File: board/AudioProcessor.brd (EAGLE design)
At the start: 49.5 x 45.7 mm, 50 parts, among them IC1 LP2951, IC2 ATTINY24/44/84-SSU, IC3 TDA7439DS, IC4 LP2951, J1 PINHD-1X3-JST-PH, J2 PINHD-1X3-JST-PH, J3 PINHD-1X3-JST-PH, J4 PINHD-1X3-JST-PH, J5 PINHD-1X6-JST-PH, J6 PINHD-1X3-JST-PH

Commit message: Removed unnecessary output biasing
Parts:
- removed C4, C8: 0.47uF, SaintGimp:CAPACITOR-5MM
- removed R6, R7, R8, R9: 10K, SaintGimp:RESISTOR-0805
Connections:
- removed net L-OUT-BIASED: C8.2, J5.2, R7.2, R9.1
- removed net R-OUT-BIASED: C4.2, J5.5, R6.2, R8.1
- net +3V3: no longer R8.2, R9.2
- net GND: no longer R6.1, R7.1
- net L-OUT: now also J5.2; no longer C8.1
- net R-OUT: now also J5.5; no longer C4.1
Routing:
- net +3V3: track 126.0 -> 100.0 mm
- net L-OUT-BIASED: track 13.2 -> 0.00 mm
- net R-OUT-BIASED: track 13.2 -> 0.00 mm
- net GND: track 44.7 -> 36.3 mm
- net L-OUT: track 20.6 -> 16.8 mm
- net R-OUT: track 14.9 -> 13.8 mm
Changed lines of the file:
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@@
 <attribute name="NAME" x="32.258" y="19.304" size="0.8128" layer="25" rot="R270"/>
-</element>
-<element name="C8" library="SaintGimp" package="CAPACITOR-5MM" value="0.47uF" x="11.43" y="15.24" smashed="yes" rot="R180">
-<attribute name="NAME" x="10.668" y="12.954" size="0.8128" layer="25"/>
-</element>
-<element name="C4" library="SaintGimp" package="CAPACITOR-5MM" value="0.47uF" x="11.43" y="25.4" smashed="yes" rot="R180">
-<attribute name="NAME" x="10.668" y="26.924" size="0.8128" layer="25"/>
 </element>
 <element name="C6" library="SaintGimp" package="CAPACITOR-1206" value="10uF" x="34.925" y="29.21" smashed="yes">
@@
 <attribute name="NAME" x="31.9405" y="7.747" size="0.8128" layer="25" rot="R270"/>
 </element>
-<element name="R6" library="SaintGimp" package="RESISTOR-0805" value="10K" x="8.89" y="21.59" smashed="yes">
-<attribute name="NAME" x="8.128" y="22.6695" size="0.8128" layer="25"/>
-</element>
 <element name="R3" library="SaintGimp" package="RESISTOR-0805" value="10K" x="35.56" y="33.02" smashed="yes" rot="R180">
 <attribute name="NAME" x="35.56" y="33.9725" size="0.8128" layer="25" rot="R180" align="top-center"/>
@@
 <element name="R11" library="SaintGimp" package="RESISTOR-0805" value="100K" x="40.64" y="19.05" smashed="yes" rot="R180">
 <attribute name="NAME" x="41.656" y="17.9705" size="0.8128" layer="25" rot="R180"/>
-</element>
-<element name="R9" library="SaintGimp" package="RESISTOR-0805" value="10K" x="13.97" y="19.05" smashed="yes">
-<attribute name="NAME" x="13.208" y="17.0815" size="0.8128" layer="25"/>
-</element>
-<element name="R7" library="SaintGimp" package="RESISTOR-0805" value="10K" x="8.89" y="19.05" smashed="yes">
-<attribute name="NAME" x="8.128" y="17.0815" size="0.8128" layer="25"/>
-</element>
-<element name="R8" library="SaintGimp" package="RESISTOR-0805" value="10K" x="13.97" y="21.59" smashed="yes">
-<attribute name="NAME" x="13.208" y="22.6695" size="0.8128" layer="25"/>
 </element>
 <element name="J6" library="SaintGimp" package="JST-B3B-PH" value="PINHD-1X3-JST-PH" x="45.72" y="24.765" smashed="yes" rot="R90">
@@
 <contactref element="R13" pad="1"/>
 <contactref element="C10" pad="2"/>
-<contactref element="R7" pad="1"/>
-<contactref element="R6" pad="1"/>
 <contactref element="C5" pad="2"/>
 <contactref element="J5" pad="4"/>
@@
 </polygon>
 <via x="35.052" y="1.27" extent="1-16" drill="0.5"/>
-<wire x1="7.89" y1="19.05" x2="7.62" y2="19.05" width="0.4064" layer="1"/>
 <via x="5.08" y="31.877" extent="1-16" drill="0.5"/>
-<wire x1="7.62" y1="19.05" x2="7.35" y2="19.32" width="0.254" layer="1"/>
-<wire x1="7.35" y1="19.32" x2="3.81" y2="19.32" width="0.254" layer="1"/>
-<wire x1="7.89" y1="21.59" x2="7.62" y2="21.32" width="0.254" layer="1"/>
-<wire x1="7.62" y1="21.32" x2="3.81" y2="21.32" width="0.254" layer="1"/>
 <via x="17.272" y="6.985" extent="1-16" drill="0.5"/>
 <wire x1="31.115" y1="23.86" x2="30.75" y2="23.495" width="0.254" layer="1"/>
@@
 <wire x1="33.925" y1="1.27" x2="33.655" y2="1.54" width="0.254" layer="1"/>
 <contactref element="C7" pad="-"/>
-<wire x1="16.145" y1="1.27" x2="46.99" y2="10.16" width="0" layer="19" extent="1-1"/>
 </signal>
 <signal name="N$3">
@@
 <wire x1="32.131" y1="28.321" x2="33.02" y2="29.21" width="0.254" layer="1"/>
 </signal>
-<signal name="L-OUT-BIASED">
-<contactref element="R9" pad="1"/>
-<contactref element="R7" pad="2"/>
-<contactref element="C8" pad="2"/>
-<contactref element="J5" pad="2"/>
-<wire x1="9.89" y1="19.05" x2="12.97" y2="19.05" width="0.254" layer="1"/>
-<wire x1="8.89" y1="15.24" x2="6.81" y2="17.32" width="0.254" layer="1"/>
-<wire x1="6.81" y1="17.32" x2="3.81" y2="17.32" width="0.254" layer="1"/>
-<wire x1="9.89" y1="19.05" x2="9.89" y2="16.24" width="0.254" layer="1"/>
-<wire x1="9.89" y1="16.24" x2="8.89" y2="15.24" width="0.254" layer="1"/>
-</signal>
 <signal name="L-OUT">
-<contactref element="C8" pad="1"/>
 <contactref element="IC3" pad="27"/>
 <wire x1="28.5242" y1="26.035" x2="28.3972" y2="26.162" width="0.254" layer="1"/>
@@
 <via x="24.892" y="22.352" extent="1-16" drill="0.5"/>
 <wire x1="24.892" y1="22.352" x2="17.78" y2="15.24" width="0.254" layer="16"/>
-<wire x1="17.78" y1="15.24" x2="13.97" y2="15.24" width="0.254" layer="16"/>
-</signal>
-<signal name="R-OUT-BIASED">
-<contactref element="R8" pad="1"/>
-<contactref element="R6" pad="2"/>
-<contactref element="C4" pad="2"/>
-<contactref element="J5" pad="5"/>
-<wire x1="9.89" y1="21.59" x2="12.97" y2="21.59" width="0.254" layer="1"/>
-<wire x1="8.89" y1="25.4" x2="6.81" y2="23.32" width="0.254" layer="1"/>
-<wire x1="6.81" y1="23.32" x2="3.81" y2="23.32" width="0.254" layer="1"/>
-<wire x1="9.89" y1="21.59" x2="9.89" y2="24.4" width="0.254" layer="1"/>
-<wire x1="9.89" y1="24.4" x2="8.89" y2="25.4" width="0.254" layer="1"/>
+<contactref element="J5" pad="2"/>
+<wire x1="3.81" y1="17.32" x2="17.78" y2="15.24" width="0" layer="19" extent="16-16"/>
 </signal>
 <signal name="R-OUT">
-<contactref element="C4" pad="1"/>
 <contactref element="IC3" pad="26"/>
-<wire x1="13.97" y1="25.4" x2="14.732" y2="24.638" width="0.254" layer="16"/>
 <wire x1="14.732" y1="24.638" x2="26.162" y2="24.638" width="0.254" layer="16"/>
 <via x="26.162" y="24.638" extent="1-16" drill="0.5"/>
 <wire x1="26.162" y1="24.638" x2="26.289" y2="24.765" width="0.254" layer="1"/>
 <wire x1="26.289" y1="24.765" x2="28.5242" y2="24.765" width="0.254" layer="1"/>
+<contactref element="J5" pad="5"/>
+<wire x1="3.81" y1="23.32" x2="14.732" y2="24.638" width="0" layer="19" extent="16-16"/>
 </signal>
 <signal name="+3V3">
-<contactref element="R9" pad="2"/>
-<contactref element="R8" pad="2"/>
 <contactref element="IC2" pad="1"/>
 <contactref element="C2" pad="2"/>
@@
 <wire x1="41.91" y1="41.91" x2="46.99" y2="36.83" width="0.254" layer="1"/>
 <wire x1="47.498" y1="33.02" x2="41.64" y2="33.02" width="0.254" layer="1"/>
-<wire x1="14.97" y1="21.59" x2="11.43" y2="25.13" width="0.254" layer="1"/>
-<wire x1="11.43" y1="25.13" x2="11.43" y2="29.21" width="0.254" layer="1"/>
-<wire x1="11.43" y1="29.21" x2="10.16" y2="30.48" width="0.254" layer="1"/>
-<wire x1="10.16" y1="30.48" x2="5.08" y2="30.48" width="0.254" layer="1"/>
-<wire x1="5.08" y1="30.48" x2="3.302" y2="32.258" width="0.254" layer="1"/>
-<wire x1="3.302" y1="32.258" x2="3.302" y2="35.052" width="0.254" layer="1"/>
-<wire x1="3.302" y1="35.052" x2="4.175" y2="35.925" width="0.254" layer="1"/>
-<wire x1="4.175" y1="35.925" x2="5.08" y2="36.325" width="0.254" layer="1"/>
-<wire x1="14.97" y1="21.59" x2="14.97" y2="19.05" width="0.254" layer="1"/>
 <wire x1="7.62" y1="36.83" x2="8.3566" y2="36.83" width="0.254" layer="1"/>
 <wire x1="8.3566" y1="35.56" x2="5.845" y2="35.56" width="0.254" layer="1"/>
@@
 <contactref element="C7" pad="+"/>
 <wire x1="45.72" y1="22.765" x2="41.1734" y2="26.035" width="0" layer="19" extent="1-1"/>
-<wire x1="46.99" y1="15.24" x2="41.1734" y2="26.035" width="0" layer="19" extent="1-1"/>
+<wire x1="46.99" y1="15.24" x2="45.72" y2="22.765" width="0" layer="19" extent="1-1"/>
 </signal>
 <signal name="N$19">

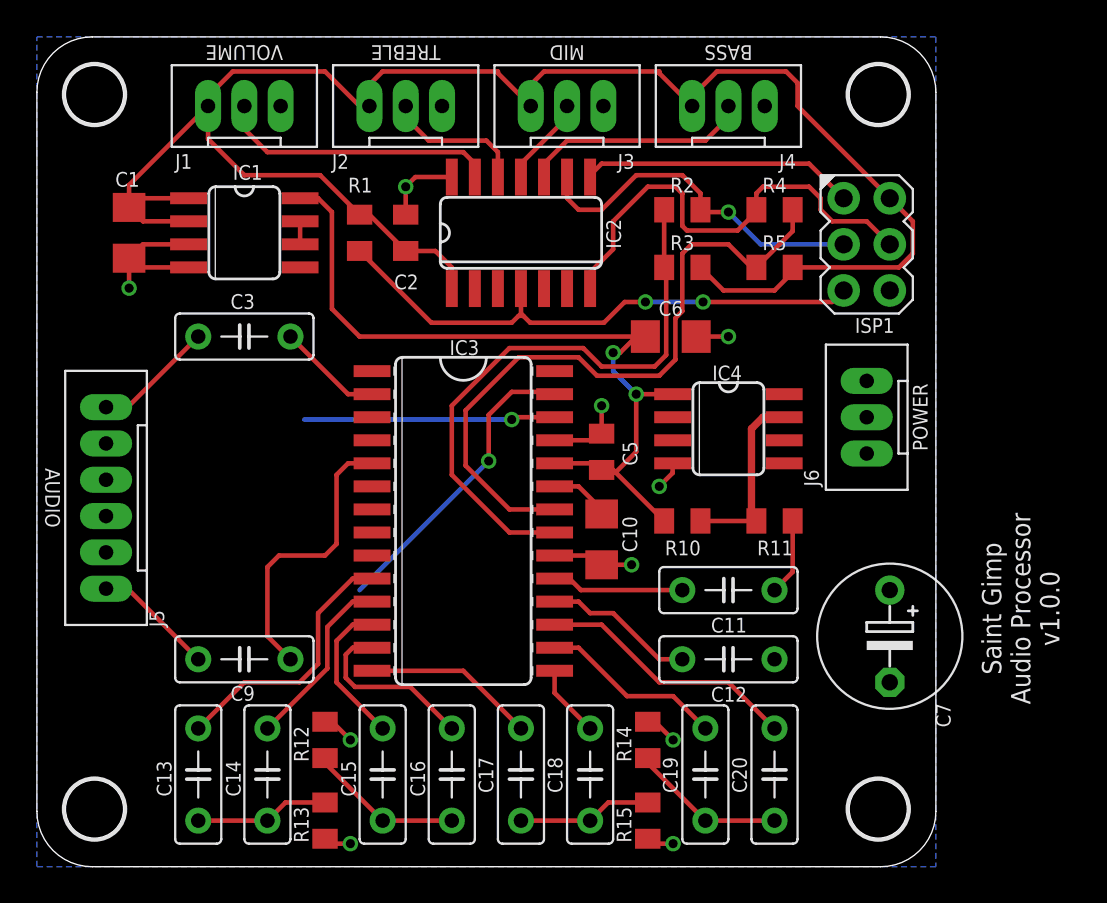
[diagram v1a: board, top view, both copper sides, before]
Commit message: Add status LED and other improvements
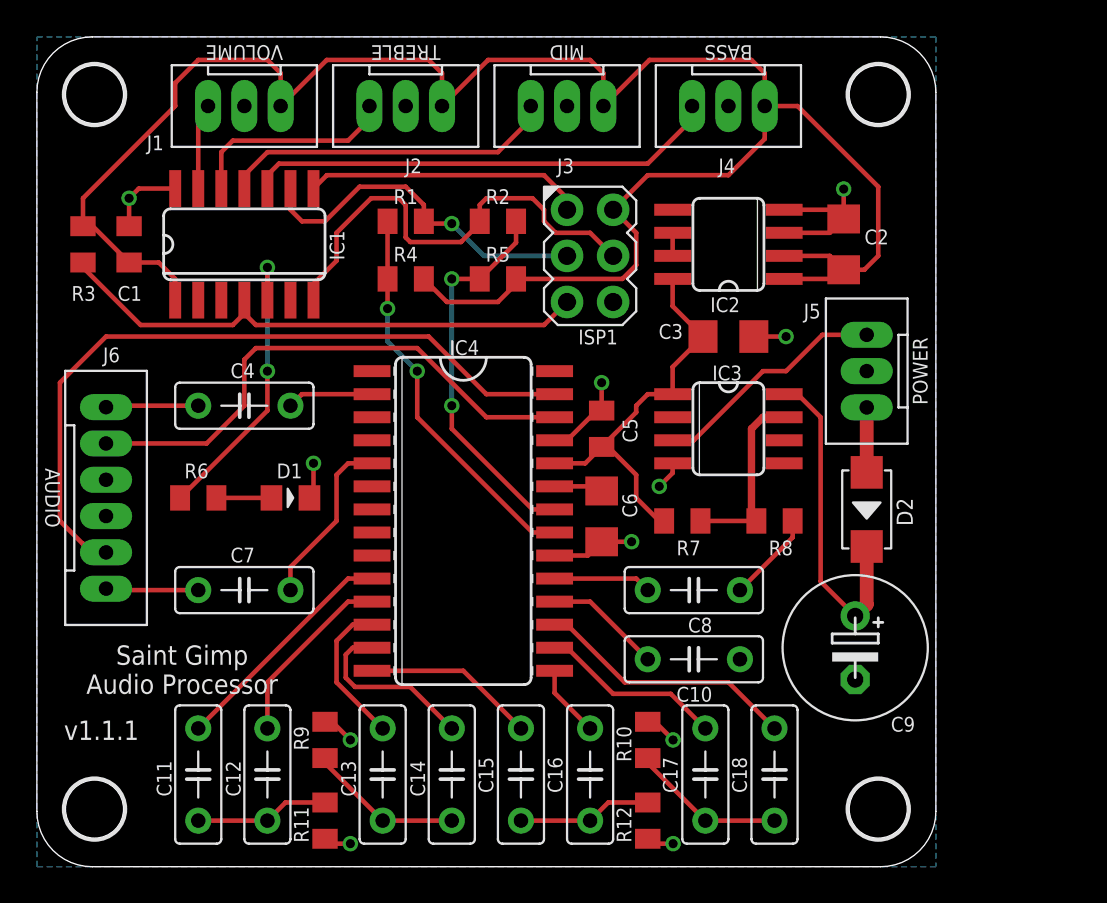
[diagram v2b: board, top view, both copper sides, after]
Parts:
- removed C19: 22nF, SaintGimp:CAPACITOR-5MM
- removed C20: 18nF, SaintGimp:CAPACITOR-5MM
- removed R13, R14: 2.7K, SaintGimp:RESISTOR-0805
- removed R15: 5.6K, SaintGimp:RESISTOR-0805
- added C4: 0.47uF, SaintGimp:CAPACITOR-5MM
- added C8: 5.6nF, SaintGimp:CAPACITOR-5MM
- added D1: LED-0805, SaintGimp:LED-0805
- added D2: DIODE-DO214AC, SaintGimp:DO-214AC
- added R6: 470, SaintGimp:RESISTOR-0805
- added R7: 620K, SaintGimp:RESISTOR-0805
- added R8: 100K, SaintGimp:RESISTOR-0805
- added R9: 5.6K, SaintGimp:RESISTOR-0805
- C1: value 10uF -> 0.1uF; device SaintGimp:CAPACITOR-1206 -> SaintGimp:CAPACITOR-0805
- C10: value 10uF -> 5.6nF; device SaintGimp:CAPACITOR-1206 -> SaintGimp:CAPACITOR-5MM
- C11: value 5.6nF -> 18nF
- C12: value 5.6nF -> 22nF
- C13: value 18nF -> 100nF
- C14: value 22nF -> 100nF
- C17: value 100nF -> 22nF
- C18: value 100nF -> 18nF
- C2: value 1uF -> 10uF; device SaintGimp:CAPACITOR-0805 -> SaintGimp:CAPACITOR-1206
- C3: value 0.47uF -> 10uF; device SaintGimp:CAPACITOR-5MM -> SaintGimp:CAPACITOR-1206
- C5: value 1uF -> 0.1uF
- C7: value 470uF -> 0.47uF; device SaintGimp:CAP-POL-5-8 -> SaintGimp:CAPACITOR-5MM
- C9: value 0.47uF -> 470uF; device SaintGimp:CAPACITOR-5MM -> SaintGimp:CAP-POL-3.5-8
- IC1: value LP2951 -> ATTINY24/44/84-SSU; device SaintGimp:SOIC-08 -> SaintGimp:SO-14
- IC2: value ATTINY24/44/84-SSU -> LP2951; device SaintGimp:SO-14 -> SaintGimp:SOIC-08
- IC3: value TDA7439DS -> LP2951; device SaintGimp:SO-28W -> SaintGimp:SOIC-08
- IC4: value LP2951 -> TDA7439DS; device SaintGimp:SOIC-08 -> SaintGimp:SO-28W
- J5: value PINHD-1X6-JST-PH -> PINHD-1X3-JST-PH; device SaintGimp:JST-B6B-PH -> SaintGimp:JST-B3B-PH
- J6: value PINHD-1X3-JST-PH -> PINHD-1X6-JST-PH; device SaintGimp:JST-B3B-PH -> SaintGimp:JST-B6B-PH
- R1: value 10K -> 470
- R10: value 620K -> 2.7K
- R11: value 100K -> 2.7K
- R4: value 470 -> 10K
- moved J5 42.5 mm to (45.7, 27.3)
- moved J6 42.1 mm to (3.81, 20.3), turned to 270 degrees
- moved C7 35.7 mm to (11.4, 15.2), turned to 0 degrees
- moved C9 33.7 mm to (45.1, 12.1), turned to 270 degrees
- moved R3 33.0 mm to (2.54, 34.3), turned to 270 degrees
- moved C11 30.9 mm to (8.89, 5.08), turned to 270 degrees
- moved R11 29.8 mm to (15.9, 2.54), turned to 90 degrees
- moved C3 26.7 mm to (38.1, 29.2)
- moved C12 26.2 mm to (12.7, 5.08), turned to 270 degrees
- moved C2 24.1 mm to (44.5, 34.3), turned to 90 degrees
- moved R4 20.7 mm to (20.3, 32.4), turned to 180 degrees
- moved R12 18.3 mm to (33.7, 2.54)
- moved IC3 15.5 mm to (38.1, 24.1)
- moved IC4 15.5 mm to (23.5, 19.1)
- moved R5 15.3 mm to (25.4, 32.4)
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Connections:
- new net LED: IC1.5, R6.2
- new net N$18: C9.+, D2.2, IC3.8
- new net N$2: D1.1, R6.1
- net +3V3: now also C1.2, C2.1, IC2.2, R4.1; no longer C1.1, C2.2, IC1.2, R1.1
- net +9V: now also C3.1, IC2.8, IC3.1, IC4.24, R7.2; no longer C6.1, IC1.8, IC3.24, IC4.1, R10.2
- net BASS: now also IC1.10, J4.3; no longer IC2.10, J4.2
- net GND: now also C1.1, C10.1, C2.2, C3.2, C8.1, C9.-, D1.2, IC1.14, IC2.3, IC2.4, IC3.4, IC4.20, IC4.25, J1.2, J2.2, J3.2, J4.2, J5.2, J6.3, J6.4, R10.2, R12.2, R8.1, R9.1; no longer C1.2, C10.2, C11.1, C12.1, C2.1, C7.-, IC1.3, IC1.4, IC2.14, IC3.20, IC3.25, IC4.4, J1.3, J2.3, J3.3, J4.3, J5.3, J5.4, J6.2, R12.1, R13.1, R14.2, R15.2
- net L-IN: now also C7.2, IC4.5; no longer C9.2, IC3.5
- net L-IN-RAW: now also C7.1, J6.6; no longer C9.1, J5.1
- net L-OUT: now also IC4.27, J6.5; no longer IC3.27, J5.2
- net MID: now also IC1.11, J3.3; no longer IC2.11, J3.2
- net MISO: now also IC1.8; no longer IC2.8
- net MOSI: now also IC1.7, R2.1; no longer IC2.7, R4.1
- net N$1: now also C10.2, IC4.18; no longer C12.2, IC3.18
- net N$10: now also C11.1, IC4.10; no longer C13.1, IC3.10
- net N$11: now also C12.1, IC4.11; no longer C14.1, IC3.11
- net N$12: now also C11.2, C12.2, R11.2; no longer C13.2, C14.2, R13.2
- net N$13: now also C13.2, C14.2, R9.2; no longer C15.2, C16.2, R12.2
- net N$14: now also C14.1, IC4.13; no longer C16.1, IC3.13
- net N$15: now also C13.1, IC4.12; no longer C15.1, IC3.12
- net N$16: now also C6.1, IC4.23; no longer C10.1, IC3.23
- net N$17: now also IC3.7, R7.1, R8.2; no longer IC4.7, R10.1, R11.2
- net N$19: now also IC2.6, IC2.7; no longer IC1.6, IC1.7
- net N$3: now also C18.2, IC4.17; no longer C20.2, IC3.17
- net N$4: now also C17.2, IC4.16; no longer C19.2, IC3.16
- net N$5: now also C17.1, C18.1, R10.1; no longer C19.1, C20.1, R14.1
- net N$6: now also C15.2, IC4.14; no longer C17.2, IC3.14
- net N$7: now also C16.2, IC4.15; no longer C18.2, IC3.15
- net N$8: now also C15.1, C16.1, R12.1; no longer C17.1, C18.1, R15.1
- net N$9: now also C8.2, IC4.19; no longer C11.2, IC3.19
- net R-IN: now also C4.2, IC4.2; no longer C3.2, IC3.2
- net R-IN-RAW: now also C4.1, J6.1; no longer C3.1, J5.6
- net R-OUT: now also IC4.26, J6.2; no longer IC3.26, J5.5
- net RST: now also IC1.4, R3.2; no longer IC2.4, R1.2
- net SCK: now also IC1.9, R1.1; no longer IC2.9, R2.1
- net SCL: now also IC4.21, R1.2, R4.2; no longer IC3.21, R2.2, R3.2
- net SDA: now also IC4.22, R2.2; no longer IC3.22, R4.2
- net SHUTDOWN: now also IC3.3, J5.3; no longer IC4.3, J6.3
- net TREBLE: now also IC1.12, J2.3; no longer IC2.12, J2.2
- net VCC: now also D2.1, J5.1; no longer C7.+, IC4.8, J6.1
- net VOLUME: now also IC1.13, J1.3; no longer IC2.13, J1.2
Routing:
- net L-OUT: track 16.8 -> 40.5 mm, vias 1 -> 0
- net +9V: track 43.9 -> 21.9 mm, vias 2 -> 0
- net N$18: track 0.00 -> 18.4 mm
- net LED: track 0.00 -> 16.5 mm, vias 0 -> 2
- net R-OUT: track 13.8 -> 30.0 mm, vias 1 -> 0
- net SDA: track 37.3 -> 21.3 mm, vias 0 -> 2
- net BASS: track 12.6 -> 26.1 mm
- net MID: track 4.96 -> 18.5 mm
- net SHUTDOWN: track 0.00 -> 13.1 mm
- net +3V3: track 100.0 -> 112.9 mm
- net SCL: track 32.6 -> 21.7 mm, vias 0 -> 2
- net VOLUME: track 15.5 -> 4.77 mm
- net L-IN: track 16.0 -> 9.62 mm
- net TREBLE: track 7.88 -> 11.6 mm
- net VCC: track 0.00 -> 3.58 mm
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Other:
- board text added: "Saint Gimp Audio Processor"
- board text added: "VIN 10-16V"
- board text added: "v1.1.1"
- board text removed: "Saint Gimp Audio Processor v1.0.0"
- board text removed: "VIN"

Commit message: Change regulator programming resistor to a value that matches house part availability and still gives us an acceptable output voltage.
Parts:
- R7: value 620K -> 680K
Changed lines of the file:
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@@
 <?xml version="1.0" encoding="utf-8"?>
 <!DOCTYPE eagle SYSTEM "eagle.dtd">
-<eagle version="8.0.0">
+<eagle version="8.3.2">
 <drawing>
 <settings>
 <setting alwaysvectorfont="no"/>
+<setting keepoldvectorfont="yes"/>
 <setting verticaltext="up"/>
 </settings>
@@
 <attribute name="NAME" x="14.1605" y="7.747" size="0.8128" layer="25" rot="R270"/>
 </element>
-<element name="R7" library="SaintGimp" package="RESISTOR-0805" value="620K" x="35.56" y="19.05" smashed="yes" rot="R180">
+<element name="R7" library="SaintGimp" package="RESISTOR-0805" value="680K" x="35.56" y="19.05" smashed="yes" rot="R180">
 <attribute name="NAME" x="36.576" y="17.9705" size="0.8128" layer="25" rot="R180"/>
 </element>
